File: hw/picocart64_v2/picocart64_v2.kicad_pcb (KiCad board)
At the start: 4 copper layers, 100 x 60 mm, 107 parts, among them J1 USB_C_Receptacle_USB2.0, J2 USB_C_Receptacle_USB2.0, J3 Conn_02x06_Odd_Even, J4 Micro_SD_Card_Det, J5 Conn_01x02, J6 Conn_01x06, Q1 FDN340P, SW1 BootButton, U1 LY68L6400SLIT, U10 USBLC6-2SC6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

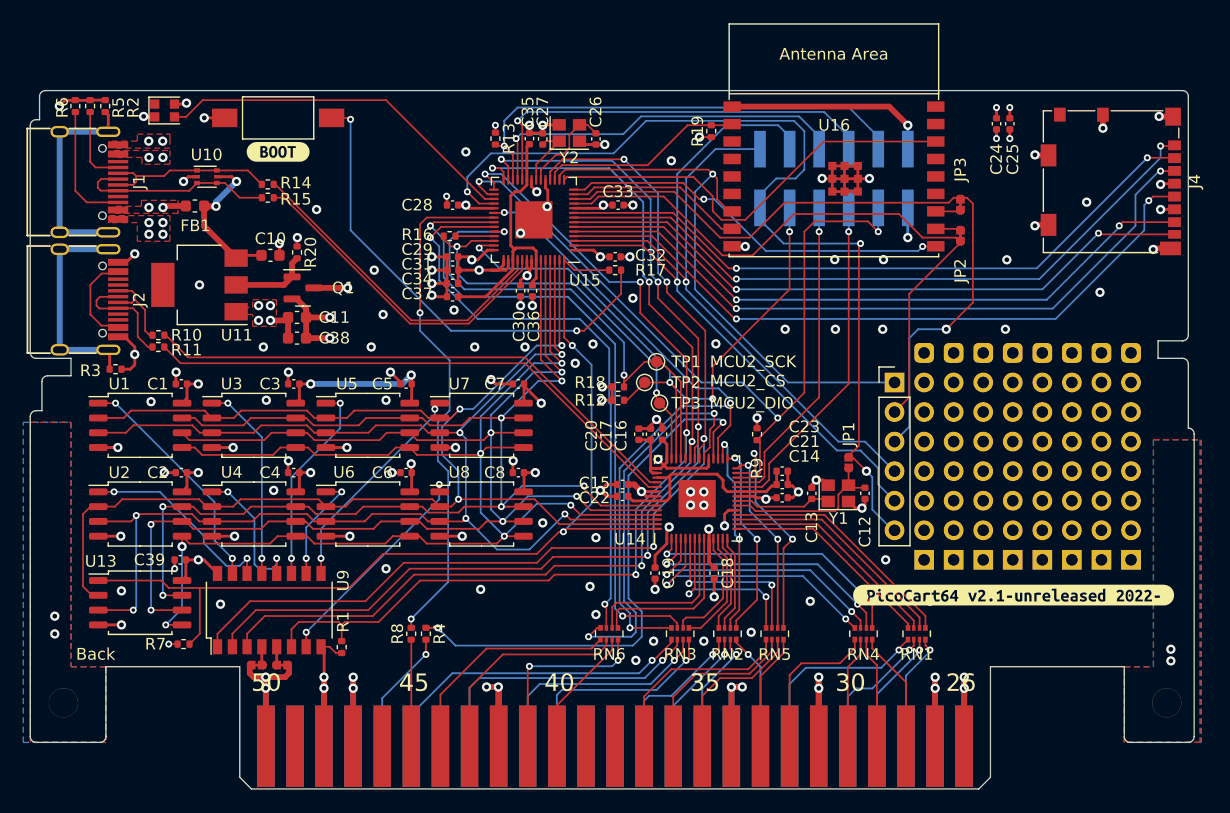
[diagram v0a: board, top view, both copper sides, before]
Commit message: hw: picocart64_v2: Added alternative LED and pin 1 markings
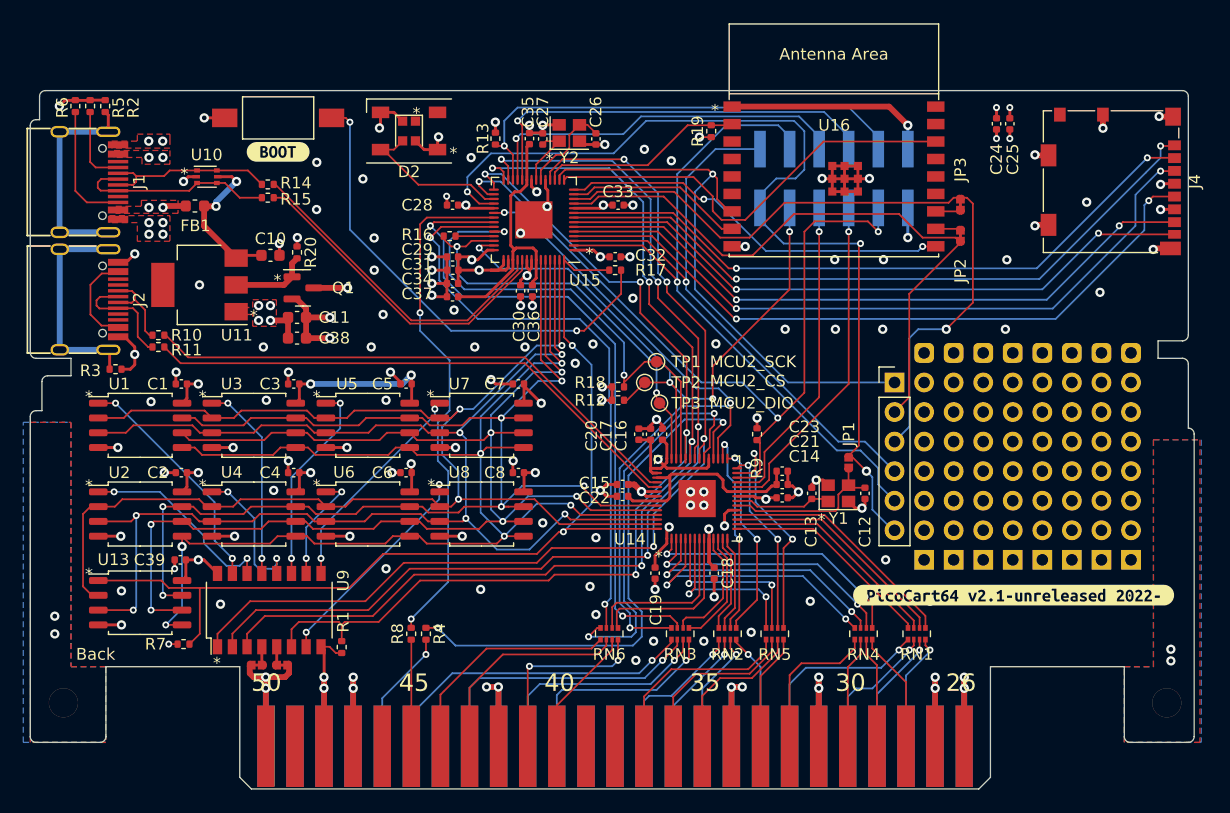
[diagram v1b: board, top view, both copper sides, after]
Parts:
- added D2: WS2812B, LED_SMD:LED_WS2812B_PLCC4_5.0x5.0mm_P3.2mm, F.Cu at (132.5, 63.5)
- moved D1 21.1 mm to (132.5, 63.5), turned to -90 degrees
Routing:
- net /Mainboard/LED: track 31.5 -> 13.7 mm
- net +3V3: track 439.0 -> 427.4 mm
- net GND: track 197.5 -> 200.1 mm, vias 135 -> 139
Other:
- board text added: "*"

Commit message: hw: picocart64_v2: Increased spacing between traces
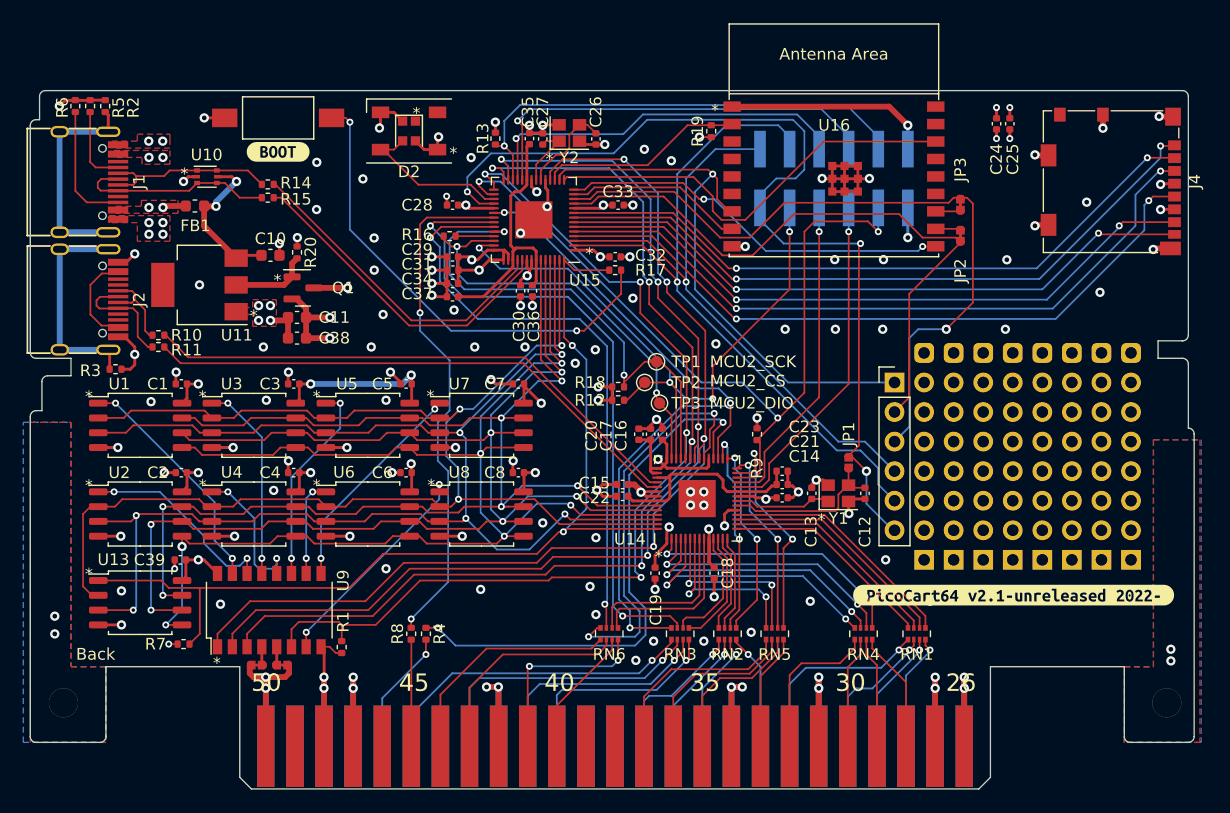
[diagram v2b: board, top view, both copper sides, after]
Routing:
- net /PSRAM Array/CS6: track 9.63 -> 8.38 mm
- net GND: track 200.1 -> 201.0 mm
- net /Mainboard/DEMUX_IE: track 84.3 -> 85.2 mm
- net +3V3: track 427.4 -> 428.1 mm
